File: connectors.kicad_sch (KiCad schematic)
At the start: 13 parts, among them J2 USB4105-GF-A, J3 Conn_02x05_Odd_Even, J5 Conn_01x02, J6 Conn_01x04, J7 STX-3120-5B-284C

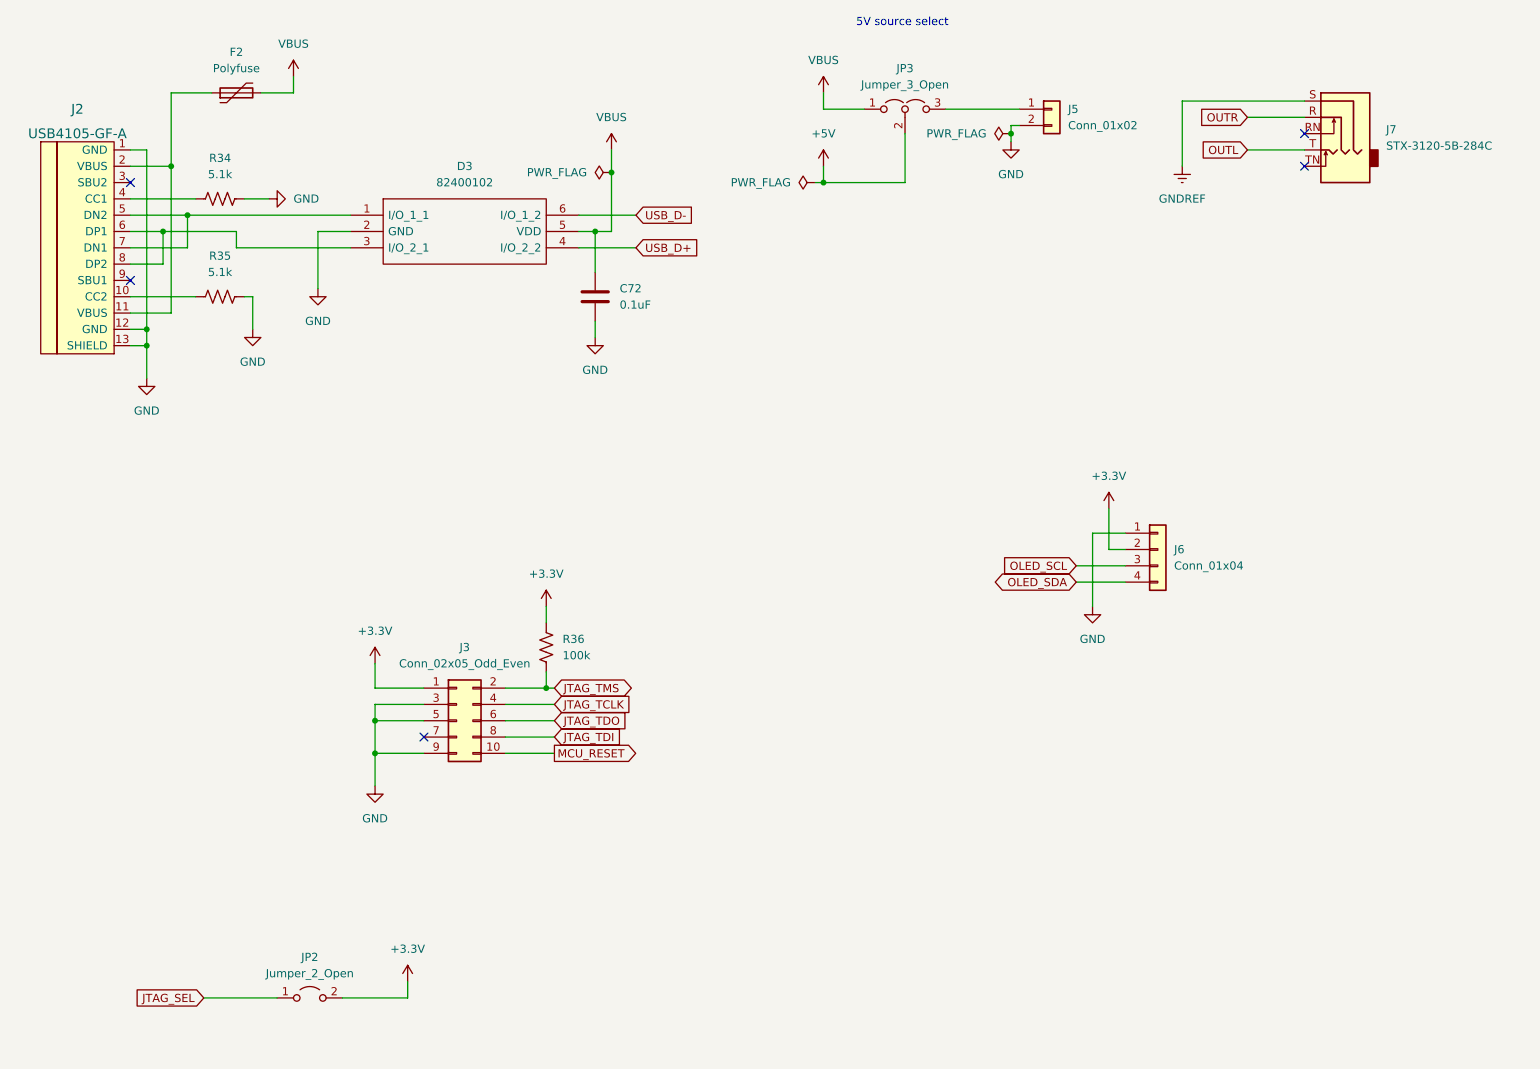
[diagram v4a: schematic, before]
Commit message: Adding footprints. WIP PCB, finished routing, no ground planes yet
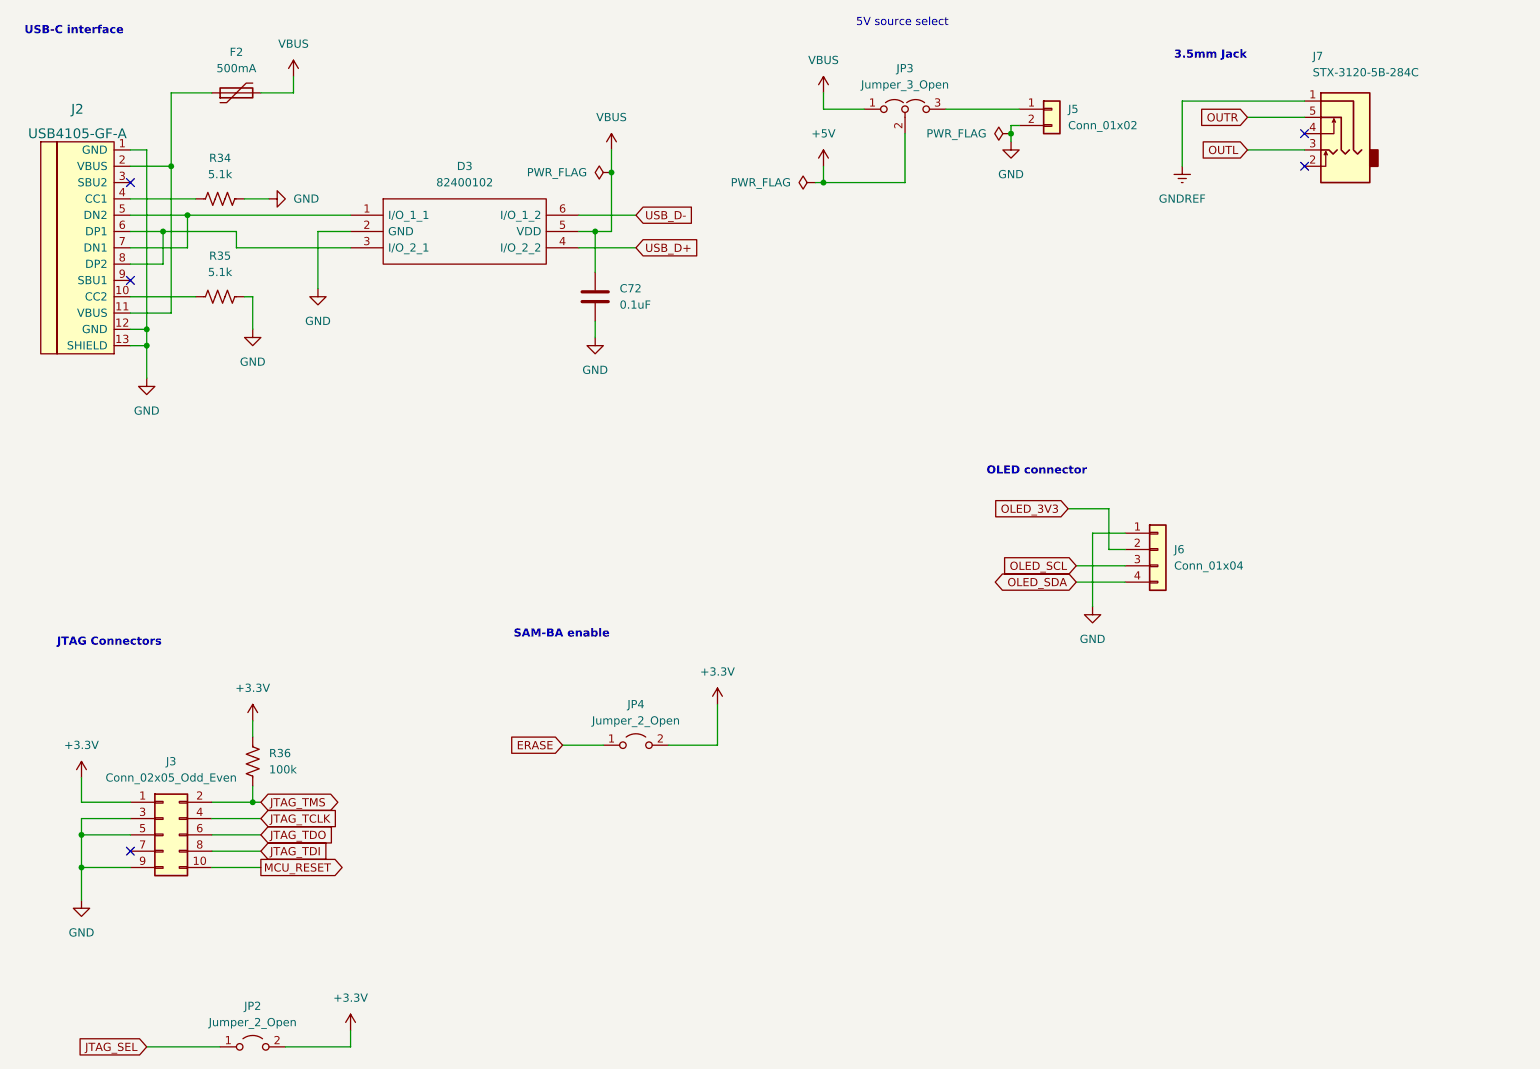
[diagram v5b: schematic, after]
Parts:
- added JP4: Jumper_2_Open, Connector_PinHeader_2.54mm:PinHeader_1x02_P2.54mm_Vertical, symbol Jumper:Jumper_2_Open
- F2: value Polyfuse -> 500mA; footprint (none) -> Fuse:Fuse_1206_3216Metric; Mouser Part number (none) -> 576-1206L050/15YR; Part Number (none) -> 1206L050/15YR
- J2: footprint (none) -> Type-C:HRO-TYPE-C-31-M-12-HandSoldering
- J3: footprint (none) -> Connector_PinHeader_2.54mm:PinHeader_2x05_P2.54mm_Vertical
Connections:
- net +3V3: now also JP4.2 (B); no longer J6.2 (Pin_2)
- net GNDREF: now also J7.1; no longer J7.S
- net OUTL: now also J7.3; no longer J7.T
- net OUTR: now also J7.5; no longer J7.R
- new net ERASE: JP4.1 (A)
- new net OLED_3V3: J6.2 (Pin_2)
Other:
- note added: "3.5mm Jack"
- note added: "JTAG Connectors"
- note added: "OLED connector"
- note added: "SAM-BA enable"
- note added: "USB-C interface"
- moved on the sheet: J3, JP2, R36

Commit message: Adding part numbers for passives
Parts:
- C72: Mouser Part Number (none) -> 187-CL21B104KBCNFNC; Part Number (none) -> CL21B104KBCNFNC
- J2: Mouser Part Number (none) -> 640-USB4105-GF-A; Part Number (none) -> USB4105-GF-A
- J7: Mouser Part Number (none) -> 806-STX-31205B284C; Part Number (none) -> STX-3120-5B-284C
- R34, R35: Mouser Part Number (none) -> 667-ERJ-6RBD5101V; Part Number (none) -> ERJ-6RBD5101V
- R36: Mouser Part Number (none) -> 71-RCV0805100KJNEA; Part Number (none) -> RCV0805100KJNEA
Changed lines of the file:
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@@
+      (effects (font (size 1.27 1.27)) hide)
+    )
+    (property "Part Number" "ERJ-6RBD5101V" (id 4) (at 55.88 43.18 90)
+      (effects (font (size 1.27 1.27)) hide)
+    )
+    (property "Mouser Part Number" "667-ERJ-6RBD5101V" (id 5) (at 55.88 43.18 90)
       (effects (font (size 1.27 1.27)) hide)
     )
@@
     )
     (property "Datasheet" "~" (id 3) (at 46.99 142.24 0)
+      (effects (font (size 1.27 1.27)) hide)
+    )
+    (property "Part Number" "" (id 4) (at 46.99 142.24 0)
+      (effects (font (size 1.27 1.27)) hide)
+    )
+    (property "Mouser Part Number" "" (id 5) (at 46.99 142.24 0)
       (effects (font (size 1.27 1.27)) hide)
     )
@@
       (effects (font (size 1.524 1.524)) hide)
     )
+    (property "Part Number" "USB4105-GF-A" (id 4) (at 39.37 49.53 0)
+      (effects (font (size 1.27 1.27)) hide)
+    )
+    (property "Mouser Part Number" "640-USB4105-GF-A" (id 5) (at 39.37 49.53 0)
+      (effects (font (size 1.27 1.27)) hide)
+    )
     (pin "1")
     (pin "10")
@@
       (effects (font (size 1.27 1.27)) hide)
     )
+    (property "Part Number" "RCV0805100KJNEA" (id 4) (at 60.96 130.81 0)
+      (effects (font (size 1.27 1.27)) hide)
+    )
+    (property "Mouser Part Number" "71-RCV0805100KJNEA" (id 5) (at 60.96 130.81 0)
+      (effects (font (size 1.27 1.27)) hide)
+    )
     (pin "1")
     (pin "2")
@@
       (effects (font (size 1.27 1.27)) hide)
     )
+    (property "Part Number" "" (id 4) (at 162.56 29.21 0)
+      (effects (font (size 1.27 1.27)) hide)
+    )
+    (property "Mouser Part Number" "" (id 5) (at 162.56 29.21 0)
+      (effects (font (size 1.27 1.27)) hide)
+    )
     (pin "1")
     (pin "2")
@@
       (effects (font (size 1.27 1.27)) hide)
     )
+    (property "Part Number" "ERJ-6RBD5101V" (id 4) (at 55.88 58.42 90)
+      (effects (font (size 1.27 1.27)) hide)
+    )
+    (property "Mouser Part Number" "667-ERJ-6RBD5101V" (id 5) (at 55.88 58.42 90)
+      (effects (font (size 1.27 1.27)) hide)
+    )
     (pin "1")
     (pin "2")
@@
     )
     (property "Datasheet" "~" (id 3) (at 185.42 29.21 0)
+      (effects (font (size 1.27 1.27)) hide)
+    )
+    (property "Part Number" "" (id 4) (at 185.42 29.21 0)
+      (effects (font (size 1.27 1.27)) hide)
+    )
+    (property "Mouser Part Number" "" (id 5) (at 185.42 29.21 0)
       (effects (font (size 1.27 1.27)) hide)
     )
@@
     )
     (property "Datasheet" "~" (id 3) (at 233.68 19.05 0)
+      (effects (font (size 1.27 1.27)) hide)
+    )
+    (property "Part Number" "STX-3120-5B-284C" (id 4) (at 229.87 30.48 0)
+      (effects (font (size 1.27 1.27)) hide)
+    )
+    (property "Mouser Part Number" "806-STX-31205B284C" (id 5) (at 229.87 30.48 0)
       (effects (font (size 1.27 1.27)) hide)
     )
@@
       (effects (font (size 1.27 1.27)) hide)
     )
+    (property "Part Number" "" (id 4) (at 201.93 97.79 0)
+      (effects (font (size 1.27 1.27)) hide)
+    )
+    (property "Mouser Part Number" "" (id 5) (at 201.93 97.79 0)
+      (effects (font (size 1.27 1.27)) hide)
+    )
     (pin "1")
     (pin "2")
@@
     )
     (property "Datasheet" "~" (id 3) (at 114.3 58.42 0)
+      (effects (font (size 1.27 1.27)) hide)
+    )
+    (property "Part Number" "CL21B104KBCNFNC" (id 4) (at 114.3 58.42 0)
+      (effects (font (size 1.27 1.27)) hide)
+    )
+    (property "Mouser Part Number" "187-CL21B104KBCNFNC" (id 5) (at 114.3 58.42 0)
       (effects (font (size 1.27 1.27)) hide)
     )
@@
       (effects (font (size 1.27 1.27)) hide)
     )
+    (property "Part Number" "" (id 4) (at 120.65 128.27 0)
+      (effects (font (size 1.27 1.27)) hide)
+    )
+    (property "Mouser Part Number" "" (id 5) (at 120.65 128.27 0)
+      (effects (font (size 1.27 1.27)) hide)
+    )

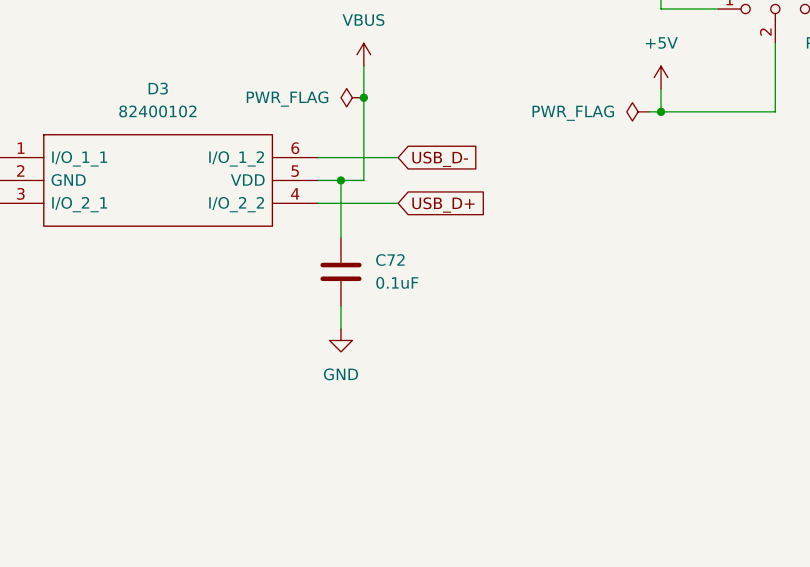
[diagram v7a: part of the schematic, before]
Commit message: Adding more part numbers. WIP verifying part numbers
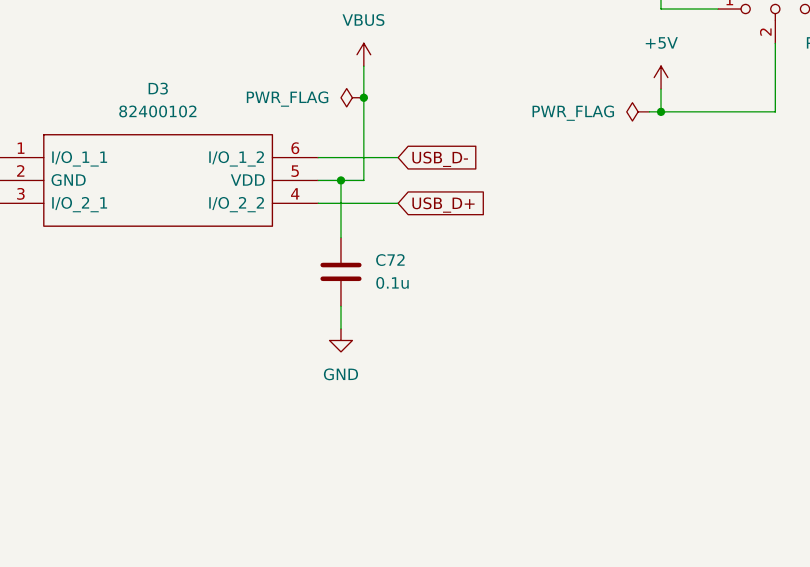
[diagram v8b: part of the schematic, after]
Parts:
- C72: value 0.1uF -> 0.1u
- F2: Mouser Part Number (none) -> 576-1206L050/15YR; Mouser Part number 576-1206L050/15YR -> (none)
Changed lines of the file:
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@@
       (effects (font (size 1.27 1.27)) hide)
     )
-    (property "Mouser Part number" "576-1206L050/15YR" (id 5) (at 58.42 26.67 90)
+    (property "Mouser Part Number" "576-1206L050/15YR" (id 5) (at 58.42 26.67 90)
       (effects (font (size 1.27 1.27)) hide)
     )
@@
       (effects (font (size 1.27 1.27)) (justify left))
     )
-    (property "Value" "0.1uF" (id 1) (at 118.11 59.6899 0)
-      (effects (font (size 1.27 1.27)) (justify left))
-    )
+    (property "Value" "0.1u" (id 1) (at 118.11 59.6899 0)
+      (effects (font (size 1.27 1.27)) (justify left))
+    )
